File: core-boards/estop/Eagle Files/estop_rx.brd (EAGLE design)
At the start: 76.2 x 50.8 mm, 29 parts, among them J1 RFM95W-3072, J2 JST-XH-02-PIN-ROUND-PAD, J3 B2PS-VH(LF)(SN), U1 R-78E5.0-1.0CONV_R-78E5.0-1.0, U4 ATMEGA328P-AUR, X6 B6B-EH-A(LF)(SN)

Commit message: estop tx design review
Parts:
- added R1: 10k, rcl:R0603
- J2: value JST-XH-02-PIN-ROUND-PAD -> B2PS-VH(LF)(SN); device IGVC-Connector:JST-XH-02-PACKAGE-ROUND-PAD -> RoboJackets-Connectors:B2PS-CENTERED
- moved J2 78.8 mm to (-4.10, 1.88), turned to 0 degrees
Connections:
- net GND: now also R1.1; no longer J1.9
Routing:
- net GND: track 45.2 -> 40.6 mm, vias 20 -> 18
- net !RESET: track 40.9 -> 36.6 mm
- net N$1: track 6.01 -> 3.86 mm
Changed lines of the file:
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@@
 <drawing>
 <settings>
-<setting alwaysvectorfont="no"/>
+<setting alwaysvectorfont="yes"/>
 <setting verticaltext="up"/>
 </settings>
@@
 <element name="JP2" library="pinhead" library_urn="urn:adsk.eagle:library:325" package="1X03" package3d_urn="urn:adsk.eagle:package:22458/2" value="Serial" x="37.749" y="48.162" smashed="yes">
 <attribute name="NAME" x="33.8628" y="49.9908" size="0.5" layer="25" ratio="10"/>
+<attribute name="POPULARITY" value="92" x="37.749" y="48.162" size="1.778" layer="27" display="off"/>
 </element>
 <element name="R10" library="resistor" library_urn="urn:adsk.eagle:library:348" package="R0603" package3d_urn="urn:adsk.eagle:package:26057/1" value="1.24k" x="58.08" y="42.328" smashed="yes" rot="R180">
@@
 <element name="R2" library="rcl" library_urn="urn:adsk.eagle:library:334" package="R0603" package3d_urn="urn:adsk.eagle:package:23555/3" value="10k" x="50.372" y="41.649" smashed="yes" rot="R90">
 <attribute name="NAME" x="48.721" y="43.046" size="0.5" layer="25" rot="R270"/>
+<attribute name="POPULARITY" value="77" x="50.372" y="41.649" size="1.778" layer="27" rot="R90" display="off"/>
 <attribute name="SPICEPREFIX" value="R" x="110.062" y="79.749" size="1.778" layer="27" rot="R90" display="off"/>
 </element>
@@
 <attribute name="VALUE" x="29.228" y="51.342" size="1.27" layer="27" font="vector" rot="R180"/>
 </element>
-<element name="J2" library="IGVC-Connector" package="JST-XH-02-PACKAGE-ROUND-PAD" value="JST-XH-02-PIN-ROUND-PAD" x="60.029" y="47.719" smashed="yes" rot="R180">
-<attribute name="NAME" x="64.284" y="49.759" size="1.016" layer="25" ratio="10" rot="R270"/>
-<attribute name="VALUE" x="63.3315" y="43.8265" size="1.016" layer="27" ratio="10" rot="R180"/>
-</element>
 <element name="U1" library="IGVC-Regulator" package="CONV_R-78E5.0-1.0" value="R-78E5.0-1.0CONV_R-78E5.0-1.0" x="71.143" y="18.948" smashed="yes" rot="R90">
 <attribute name="NAME" x="66.063" y="13.233" size="1.27" layer="25" rot="R90"/>
@@
 <attribute name="MPN" value="B2PS-VH(LF)(SN)" x="71.153" y="7.856" size="1.778" layer="27" display="off"/>
 <attribute name="NAME" x="71.153" y="9.706" size="1" layer="25" font="vector" ratio="10" align="bottom-center"/>
+</element>
+<element name="R1" library="rcl" library_urn="urn:adsk.eagle:library:334" package="R0603" package3d_urn="urn:adsk.eagle:package:23555/3" value="10k" x="1.5" y="-3.01" smashed="yes">
+<attribute name="NAME" x="0.865" y="-2.375" size="1.27" layer="25"/>
+<attribute name="POPULARITY" value="77" x="1.5" y="-3.01" size="1.778" layer="27" display="off"/>
+<attribute name="SPICEPREFIX" value="R" x="1.5" y="-3.01" size="1.778" layer="27" display="off"/>
+<attribute name="VALUE" x="0.865" y="-4.915" size="1.27" layer="27"/>
+</element>
+<element name="J2" library="RoboJackets-Connectors" package="B2PS-CENTERED" value="B2PS-VH(LF)(SN)" x="-4.1" y="1.88" smashed="yes">
+<attribute name="DIGIKEY" value="455-1648-ND" x="-4.1" y="1.88" size="1.778" layer="27" display="off"/>
+<attribute name="MPN" value="B2PS-VH(LF)(SN)" x="-4.1" y="1.88" size="1.778" layer="27" display="off"/>
+<attribute name="NAME" x="-4.1" y="3.73" size="1" layer="25" font="vector" ratio="10" align="bottom-center"/>
 </element>
 </elements>
@@
 <contactref element="JP2" pad="3"/>
 <contactref element="J1" pad="2"/>
-<contactref element="J1" pad="9"/>
-<contactref element="J2" pad="2"/>
 <contactref element="U4" pad="21"/>
 <contactref element="C4" pad="2"/>
@@
 <wire x1="73.718" y1="27" x2="74.8058" y2="27" width="0.4064" layer="1"/>
 <via x="74.8058" y="27" extent="1-16" drill="0.35"/>
-<wire x1="58.759" y1="47.719" x2="57.719" y2="47.719" width="0.4064" layer="1"/>
-<wire x1="57.719" y1="47.719" x2="57" y2="47" width="0.4064" layer="1"/>
-<via x="57" y="47" extent="1-16" drill="0.35"/>
 <wire x1="47.839" y1="45.436" x2="46.736" y2="45.436" width="0.4064" layer="1"/>
 <wire x1="46.736" y1="45.436" x2="46.2" y2="44.9" width="0.4064" layer="1"/>
@@
 <wire x1="27.079" y1="29" x2="26" y2="29" width="0.4064" layer="1"/>
 <via x="26" y="29" extent="1-16" drill="0.35"/>
-<wire x1="27.45" y1="47.151" x2="27.299" y2="47" width="0.4064" layer="1"/>
-<wire x1="27.299" y1="47" x2="25" y2="47" width="0.4064" layer="1"/>
-<via x="25" y="47" extent="1-16" drill="0.35"/>
 <wire x1="26.886" y1="9.871" x2="28" y2="8.757" width="0.4064" layer="1"/>
 <wire x1="28" y1="8.757" x2="28" y2="7" width="0.4064" layer="1"/>
@@
 <wire x1="46.3484" y1="49.06" x2="46.4084" y2="49" width="0.4064" layer="1"/>
 <via x="46.4084" y="49" extent="1-16" drill="0.35"/>
+<contactref element="R1" pad="1"/>
+<contactref element="J2" pad="2"/>
+<wire x1="57.508" y1="38.492" x2="69.89" y2="39.926" width="0" layer="19" extent="1-1"/>
+<wire x1="57.23" y1="42.328" x2="57" y2="39" width="0" layer="19" extent="1-1"/>
+<wire x1="54.7655" y1="34.814" x2="57.508" y2="37.09" width="0" layer="19" extent="1-1"/>
+<wire x1="57.523" y1="31.427" x2="54.7655" y2="34.814" width="0" layer="19" extent="1-1"/>
+<wire x1="48" y1="35" x2="53" y2="35" width="0" layer="19" extent="1-1"/>
+<wire x1="47.986" y1="34.014" x2="48" y2="35" width="0" layer="19" extent="1-1"/>
+<wire x1="47.839" y1="45.436" x2="56" y2="43" width="0" layer="19" extent="1-1"/>
+<wire x1="46.4084" y1="49" x2="46.736" y2="45.436" width="0" layer="19" extent="1-1"/>
+<wire x1="42.46" y1="48.18" x2="44.679" y2="49.06" width="0" layer="19" extent="1-1"/>
+<wire x1="73.718" y1="27" x2="69.89" y2="39.926" width="0" layer="19" extent="1-1"/>
+<wire x1="73.393" y1="19" x2="73.718" y2="26.903" width="0" layer="19" extent="1-1"/>
+<wire x1="67" y1="11" x2="72" y2="19" width="0" layer="19" extent="1-1"/>
+<wire x1="73.133" y1="7.856" x2="67" y2="11" width="0" layer="19" extent="1-1"/>
+<wire x1="35.282" y1="23.967" x2="44.934" y2="34.19" width="0" layer="19" extent="1-1"/>
+<wire x1="35.046" y1="14.723" x2="34.765" y2="18" width="0" layer="19" extent="1-1"/>
+<wire x1="28" y1="8.757" x2="35.046" y2="14.723" width="0" layer="19" extent="1-1"/>
+<wire x1="26.178" y1="2.117" x2="28" y2="7" width="0" layer="19" extent="1-1"/>
+<wire x1="21.374" y1="2.374" x2="26.178" y2="2.117" width="0" layer="19" extent="1-1"/>
+<wire x1="27.45" y1="29.371" x2="35.282" y2="23.967" width="0" layer="19" extent="1-1"/>
+<wire x1="0.65" y1="-3.01" x2="21" y2="2" width="0" layer="19" extent="1-1"/>
+<wire x1="-2.12" y1="1.88" x2="0.65" y2="-3.01" width="0" layer="19" extent="1-1"/>
 </signal>
 <signal name="MISO">
@@
 <signal name="!RESET">
 <contactref element="PROG" pad="!RESET"/>
-<contactref element="R2" pad="1"/>
 <contactref element="U4" pad="29"/>
 <contactref element="C6" pad="1"/>
@@
 <wire x1="72.43" y1="39.926" x2="71.3124" y2="41.0436" width="0.254" layer="1"/>
 <wire x1="45.5936" y1="41.4064" x2="49.7646" y2="41.4064" width="0.254" layer="1"/>
-<wire x1="49.7646" y1="41.4064" x2="50.372" y2="40.799" width="0.254" layer="1"/>
 <wire x1="51.171" y1="40" x2="68.38346875" y2="40" width="0.254" layer="1"/>
 <wire x1="50.372" y1="38.4555" x2="50.338" y2="38.4215" width="0.254" layer="1"/>
-<wire x1="50.372" y1="40.799" x2="50.372" y2="38.4555" width="0.254" layer="1"/>
-<wire x1="50.372" y1="40.799" x2="51.171" y2="40" width="0.254" layer="1"/>
 <wire x1="46.063" y1="47.36" x2="47.839" y2="49.136" width="0.254" layer="1"/>
+<contactref element="R2" pad="1"/>
+<wire x1="50.372" y1="40.799" x2="51.171" y2="40" width="0" layer="19" extent="1-1"/>
+<wire x1="49.7646" y1="41.4064" x2="50.372" y2="40.799" width="0" layer="19" extent="1-1"/>
+<wire x1="50.372" y1="38.4555" x2="51.171" y2="40" width="0" layer="19" extent="1-1"/>
 </signal>
 <signal name="N$2">
@@
 <vertex x="63.52" y="17.75"/>
 <vertex x="64.64" y="17.75"/>
-<vertex x="64.64" y="17.75"/>
 <vertex x="76.01" y="17.75"/>
 <vertex x="76.01" y="50.53"/>
@@
 <signal name="N$1">
 <contactref element="R9" pad="1"/>
+<wire x1="62.815" y1="46.203" x2="62.815" y2="42.339" width="0.254" layer="1"/>
 <contactref element="J2" pad="1"/>
-<wire x1="61.299" y1="47.719" x2="62.815" y2="46.203" width="0.254" layer="1"/>
-<wire x1="62.815" y1="46.203" x2="62.815" y2="42.339" width="0.254" layer="1"/>
+<wire x1="-6.08" y1="1.88" x2="62.815" y2="42.339" width="0" layer="19" extent="1-1"/>
 </signal>
 <signal name="+12V">

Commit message: final tm edits for design review
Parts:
- removed JP2: Serial, pinhead:1X03
- added C7: 0.1uF, rcl:C0603
- added U$2: (no value), RoboJackets-Aesthetics:ROBOBUZZ_1.0X2
- added U2: MCP2551T-E/SN, IGVC-Microcontroller:SOIC8-N_MC
- added X1: JST-XH-03-PIN-ROUND-PAD, IGVC-Connector:JST-XH-03-PACKAGE-ROUND-PAD
- moved J2 62.7 mm to (58.3, 7.93)
- moved R1 57.5 mm to (32.1, 45.7), turned to 90 degrees
- moved R9 30.2 mm to (56.4, 12.6), turned to 0 degrees
- moved R10 29.8 mm to (60.5, 12.6), turned to 0 degrees
- moved C6 11.8 mm to (56.5, 47.9)
- moved S3 11.2 mm to (62.1, 46.8)
- moved R2 6.47 mm to (56.4, 44.0)
- moved C5 1.87 mm to (71.0, 27.0)
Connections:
- removed net RX: JP2.2, U4.30
- removed net TX: JP2.1, U4.31
- new net CAN_N: U2.6, X1.2
- new net CAN_P: U2.7, X1.3
- new net CAN_RX: U2.4, U4.30
- new net CAN_TX: U2.1, U4.31
- new net N$5: J1.9, R1.2
- net +5V: now also C7.1, U2.3, X1.1
- net CE: now also U4.14; no longer U4.7
- net GND: now also C7.2, U2.2, U2.8; no longer JP2.3
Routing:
- net TX: track 19.9 -> 0.00 mm
- net RX: track 18.1 -> 0.00 mm
- net CE: track 27.6 -> 40.8 mm
- net CAN_N: track 0.00 -> 11.9 mm
- net CAN_P: track 0.00 -> 10.0 mm
- net GND: track 40.6 -> 48.8 mm, vias 18 -> 21
- net +5V: track 0.00 -> 5.17 mm
- net N$5: track 0.00 -> 4.88 mm
- net MISO: track 65.6 -> 61.6 mm, vias 4 -> 0
- net CAN_RX: track 0.00 -> 3.80 mm
- net !RESET: track 36.6 -> 33.4 mm
- net CAN_TX: track 0.00 -> 3.17 mm
- net SCK: track 66.4 -> 64.5 mm, vias 2 -> 3
- net N$1: track 3.86 -> 4.99 mm
- net IN: track 52.5 -> 53.6 mm
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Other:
- board text added: "BUTTON"
- board text added: "CAN"
- board text added: "E-STOP IN"
- board text added: "E-Stop Board RX"
- board text added: "POWER"
- board text added: "POWER IN"
- board text added: "RoboJackets IGVC"
- board text added: "WIRELESS"
- board text added: "v1.2"

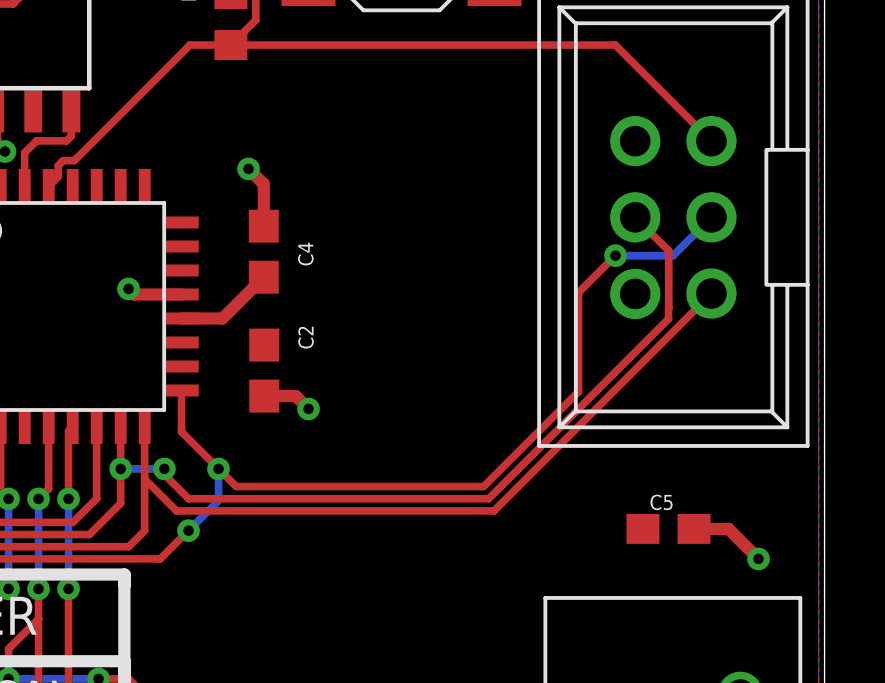
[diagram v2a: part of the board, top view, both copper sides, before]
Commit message: fixed 5v airwire
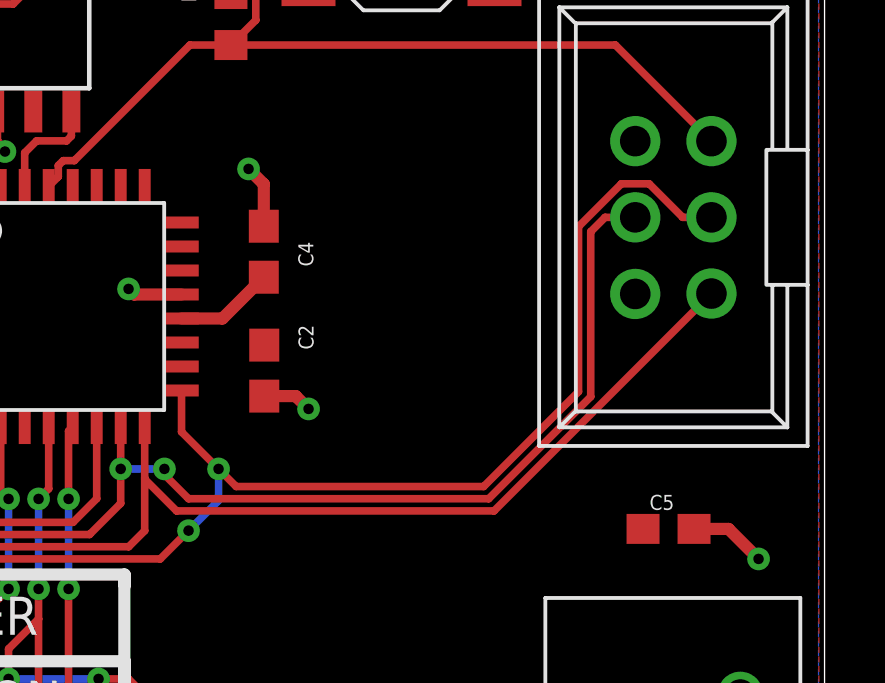
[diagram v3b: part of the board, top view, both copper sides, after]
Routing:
- net SCK: track 64.5 -> 66.7 mm, vias 3 -> 2
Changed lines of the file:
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@@
 <wire x1="29.7429375" y1="37.8128" x2="32.336675" y2="37.8128" width="0.254" layer="1"/>
 <wire x1="33.8128" y1="36.336675" x2="33.8128" y2="29.3619375" width="0.254" layer="1"/>
-<wire x1="71.0076" y1="34.36906875" x2="71" y2="34.36146875" width="0.254" layer="1"/>
-<wire x1="71" y1="34.36146875" x2="71" y2="34" width="0.254" layer="1"/>
-<wire x1="69.89" y1="37.386" x2="71.0076" y2="36.2684" width="0.254" layer="1"/>
-<wire x1="71.0076" y1="36.2684" x2="71.0076" y2="34.36906875" width="0.254" layer="1"/>
-<wire x1="71" y1="34" x2="65.0064" y2="28.0064" width="0.254" layer="1"/>
-<wire x1="65.0064" y1="28.0064" x2="55" y2="28.0064" width="0.254" layer="1"/>
+<wire x1="55" y1="28.0064" x2="65.0064" y2="28.0064" width="0.254" layer="1"/>
 <wire x1="55" y1="28.0064" x2="54.1956" y2="28.8108" width="0.254" layer="1"/>
 <wire x1="54.1956" y1="28.8108" x2="54.1956" y2="29" width="0.254" layer="1"/>
@@
 <wire x1="54.1956" y1="29" x2="52.738" y2="29" width="0.254" layer="16"/>
 <via x="52.738" y="29" extent="1-16" drill="0.35"/>
+<wire x1="68.4064" y1="31.4064" x2="68.4064" y2="36.90819375" width="0.254" layer="1"/>
+<wire x1="65.0064" y1="28.0064" x2="68.4064" y2="31.4064" width="0.254" layer="1"/>
+<wire x1="68.4064" y1="36.90819375" x2="68.88420625" y2="37.386" width="0.254" layer="1"/>
+<wire x1="68.88420625" y1="37.386" x2="69.89" y2="37.386" width="0.254" layer="1"/>
 </signal>
 <signal name="SCK">
@@
 <wire x1="33" y1="36" x2="33" y2="29" width="0.254" layer="1"/>
 <wire x1="33" y1="29" x2="36" y2="26" width="0.254" layer="1"/>
-<wire x1="72.43" y1="37.386" x2="71.153" y2="36.109" width="0.254" layer="16"/>
-<wire x1="71.153" y1="36.109" x2="69.23121875" y2="36.109" width="0.254" layer="16"/>
-<via x="69.23121875" y="36.109" extent="1-16" drill="0.35"/>
-<wire x1="69.23121875" y1="36.109" x2="68" y2="34.87778125" width="0.254" layer="1"/>
-<wire x1="68" y1="34.87778125" x2="68" y2="31.5747375" width="0.254" layer="1"/>
-<wire x1="68" y1="31.5747375" x2="64.8380625" y2="28.4128" width="0.254" layer="1"/>
+<wire x1="64.8380625" y1="28.4128" x2="68" y2="31.5747375" width="0.254" layer="1"/>
 <wire x1="54.0576" y1="26" x2="55" y2="26.9424" width="0.254" layer="1"/>
 <via x="55" y="26.9424" extent="1-16" drill="0.35"/>
@@
 <wire x1="56" y1="29" x2="54.7655" y2="30.2345" width="0.254" layer="1"/>
 <wire x1="54.7655" y1="30.2345" x2="54.7655" y2="31.614" width="0.254" layer="1"/>
+<wire x1="69.42706875" y1="38.5036" x2="70.35293125" y2="38.5036" width="0.254" layer="1"/>
+<wire x1="71.47053125" y1="37.386" x2="72.43" y2="37.386" width="0.254" layer="1"/>
+<wire x1="70.35293125" y1="38.5036" x2="71.47053125" y2="37.386" width="0.254" layer="1"/>
+<wire x1="68" y1="37.07653125" x2="69.42706875" y2="38.5036" width="0.254" layer="1"/>
+<wire x1="68" y1="31.5747375" x2="68" y2="37.07653125" width="0.254" layer="1"/>
 </signal>
 <signal name="!RESET">
@@
 <contactref element="C5" pad="1"/>
 <contactref element="PROG" pad="+5V"/>
-<wire x1="69.89" y1="34.832" x2="70.15" y2="27" width="0" layer="19" extent="1-1"/>
 </signal>
 <signal name="N$1">

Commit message: almost order ready haha
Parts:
- removed X1: JST-XH-03-PIN-ROUND-PAD, IGVC-Connector:JST-XH-03-PACKAGE-ROUND-PAD
- removed X6: B6B-EH-A(LF)(SN), IGVC-Connector:B6BEHALFSN
- added J4: 2-PIN_2MM-V, RoboJackets-Connectors:2MM-2-V
- added J5: 6-PIN_2MM-V, RoboJackets-Connectors:2MM-6-V
- added R7: 10k, rcl:R0603
- moved C5 9.22 mm to (65.0, 20.0), turned to 90 degrees
- moved D12 2.66 mm to (7.09, 12.4)
- moved D14 2.08 mm to (23.3, 11.9)
- moved D13 1.68 mm to (14.5, 20.1)
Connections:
- new net EN: U4.11
- new net N$6: J1.3, R7.2
- net +24V: now also J5.1; no longer X6.X-1
- net +5V: now also R7.1; no longer X1.1
- net CAN_N: now also J4.2; no longer X1.2
- net CAN_P: now also J4.1; no longer X1.3
- net DIODE_TO_GREEN: now also J5.2; no longer X6.X-2
- net DIODE_TO_INTER: now also J5.4; no longer X6.X-4
- net GND: now also J5.6; no longer X6.X-6
- net MOTOR_POWER: now also J5.3; no longer X6.X-3
- net SOLENOID_TRIG: now also J5.5; no longer X6.X-5
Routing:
- net IN: track 53.6 -> 47.2 mm, vias 4 -> 3
- net +5V: track 5.17 -> 0.00 mm
- net SOLENOID_TRIG: track 37.6 -> 42.2 mm
- net N$6: track 0.00 -> 3.97 mm
- net +24V: track 8.61 -> 12.0 mm
- net DIODE_TO_GREEN: track 6.58 -> 9.73 mm
- net GND: track 48.8 -> 46.4 mm
- net MOTOR_POWER: track 16.1 -> 18.2 mm
- net CAN_P: track 10.0 -> 12.1 mm
- net CAN_N: track 11.9 -> 10.3 mm
- net DIODE_TO_INTER: track 16.2 -> 17.8 mm
- net WIRELESS_LED: track 15.1 -> 15.7 mm
